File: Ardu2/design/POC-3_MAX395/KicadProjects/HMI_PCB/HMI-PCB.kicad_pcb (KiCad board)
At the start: 2 copper layers, 170.2 x 71.6 mm, 41 parts, among them P1 SplitPot_0_M, P10 TREM_VIB, P11 SplitPot_5_TR, P12 Analog Power IN, P13 Digital Power IN/OUT, P2 SEQ_SAVE, P3 SplitPot_1_A, P4 SplitPot_2_B, P5 PB_OUT, P6 Analog_Out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

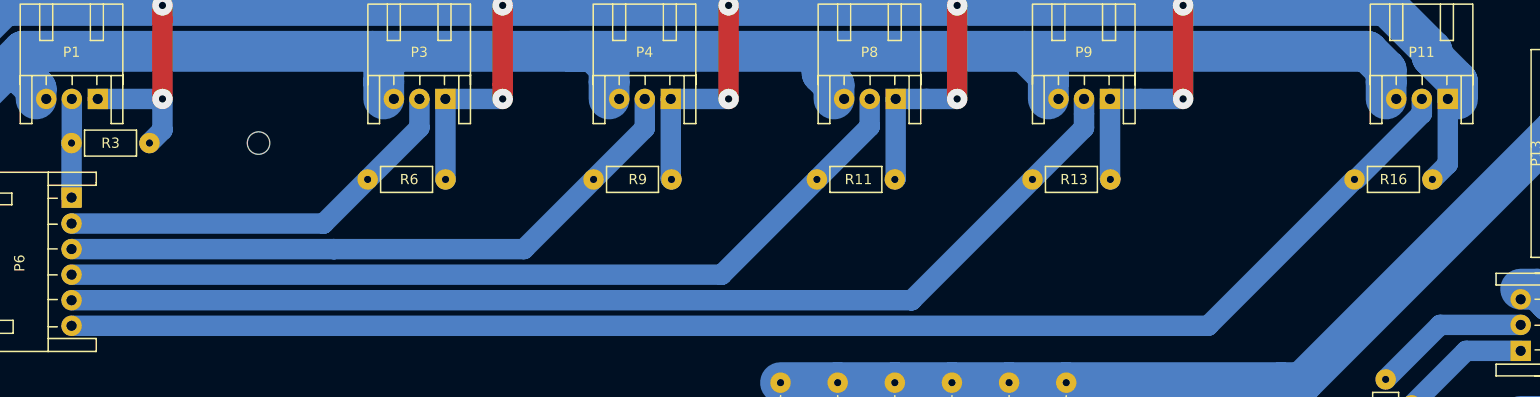
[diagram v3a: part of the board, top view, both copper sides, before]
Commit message: updated peripherals PCB
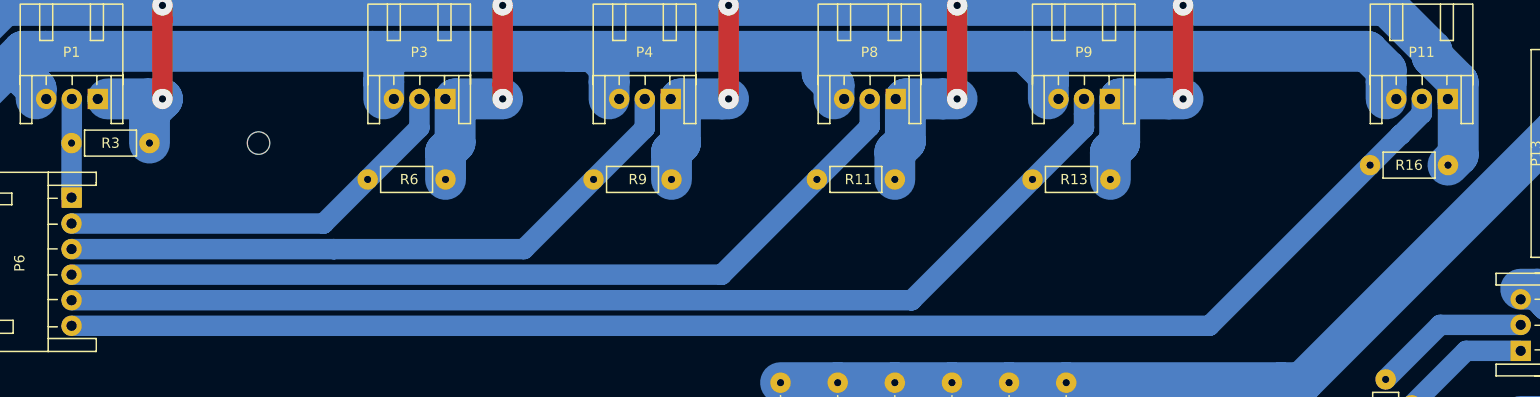
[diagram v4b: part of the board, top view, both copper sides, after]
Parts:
- moved R16 2.07 mm to (210.6, 92.3)
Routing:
- net /GND_A: track 281.5 -> 278.3 mm
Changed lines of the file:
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@@
     (thickness 1.6)
     (drawings 22)
-    (tracks 199)
+    (tracks 208)
     (zones 0)
     (modules 41)
@@
   )
   (module misc:Resistor_Horizontal_RM7mm_Big_Pads (layer F.Cu)
-    (at 209.042 93.726)
+    (at 210.566 92.329)
     (descr "Resistor, Axial,  RM 7.62mm, 1/3W,")
     (tags "Resistor Axial RM 7.62mm 1/3W R3")
@@
   (segment (start 165.5245 120.9875) (end 152.908 133.604) (width 2) (layer B.Cu) (net 7) (status 20))
   (segment (start 152.908 133.604) (end 152.908 135.641) (width 2) (layer B.Cu) (net 7) (status 30))
+  (segment (start 120.142 93.726) (end 120.142 91.041619) (width 4) (layer B.Cu) (net 8))
+  (segment (start 121.07801 90.105609) (end 121.07801 85.852) (width 4) (layer B.Cu) (net 8))
+  (segment (start 120.142 91.041619) (end 121.07801 90.105609) (width 4) (layer B.Cu) (net 8))
+  (segment (start 125.73 85.852) (end 121.07801 85.852) (width 4) (layer B.Cu) (net 8))
+  (segment (start 91.186 90.17) (end 91.186 87.122) (width 4) (layer B.Cu) (net 8))
+  (segment (start 91.186 87.122) (end 92.456 85.852) (width 4) (layer B.Cu) (net 8))
+  (segment (start 92.456 85.852) (end 91.041787 85.852) (width 4) (layer B.Cu) (net 8))
+  (segment (start 91.041787 85.852) (end 87.07801 85.852) (width 4) (layer B.Cu) (net 8))
+  (segment (start 142.24 93.726) (end 142.24 91.041619) (width 4) (layer B.Cu) (net 8))
+  (segment (start 142.24 91.041619) (end 143.11801 90.163609) (width 4) (layer B.Cu) (net 8))
+  (segment (start 143.11801 90.163609) (end 143.11801 85.852) (width 4) (layer B.Cu) (net 8))
+  (segment (start 147.828 85.852) (end 147.193 85.852) (width 4) (layer B.Cu) (net 8))
+  (segment (start 147.193 85.852) (end 143.11801 85.852) (width 4) (layer B.Cu) (net 8))
+  (segment (start 164.084 93.726) (end 164.084 91.041619) (width 4) (layer B.Cu) (net 8))
+  (segment (start 164.084 91.041619) (end 165.11801 90.007609) (width 4) (layer B.Cu) (net 8))
+  (segment (start 165.11801 90.007609) (end 165.11801 85.852) (width 4) (layer B.Cu) (net 8))
+  (segment (start 170.18 85.852) (end 168.765787 85.852) (width 4) (layer B.Cu) (net 8))
+  (segment (start 168.765787 85.852) (end 165.11801 85.852) (width 4) (layer B.Cu) (net 8))
+  (segment (start 185.166 93.726) (end 185.166 91.041619) (width 4) (layer B.Cu) (net 8))
+  (segment (start 185.166 91.041619) (end 186.078019 90.1296) (width 4) (layer B.Cu) (net 8))
+  (segment (start 186.078019 90.1296) (end 186.078019 85.852) (width 4) (layer B.Cu) (net 8))
+  (segment (start 192.278 85.852) (end 190.863787 85.852) (width 4) (layer B.Cu) (net 8))
+  (segment (start 190.863787 85.852) (end 186.078019 85.852) (width 4) (layer B.Cu) (net 8))
+  (segment (start 219.118001 84.176799) (end 219.185999 84.244797) (width 4) (layer B.Cu) (net 8))
+  (segment (start 219.185999 84.244797) (end 219.185999 91.329001) (width 4) (layer B.Cu) (net 8))
+  (segment (start 219.185999 91.329001) (end 218.186 92.329) (width 4) (layer B.Cu) (net 8))
   (segment (start 92.456 76.708) (end 76.962 76.708) (width 4) (layer B.Cu) (net 8))
   (segment (start 76.962 76.708) (end 69.881991 83.788009) (width 4) (layer B.Cu) (net 8))
   (segment (start 69.881991 83.788009) (end 69.881991 86.614) (width 4) (layer B.Cu) (net 8) (status 20))
-  (segment (start 218.168 85.852) (end 218.168 92.22) (width 2) (layer B.Cu) (net 8) (status 10))
-  (segment (start 218.168 92.22) (end 216.662 93.726) (width 2) (layer B.Cu) (net 8) (status 20))
-  (segment (start 120.128 85.852) (end 125.73 85.852) (width 2) (layer B.Cu) (net 8) (status 10))
-  (segment (start 164.168 85.852) (end 164.168 93.642) (width 2) (layer B.Cu) (net 8) (status 30))
-  (segment (start 164.168 93.642) (end 164.084 93.726) (width 2) (layer B.Cu) (net 8) (status 30))
-  (segment (start 142.168 85.852) (end 142.168 93.654) (width 2) (layer B.Cu) (net 8) (status 30))
-  (segment (start 142.168 93.654) (end 142.24 93.726) (width 2) (layer B.Cu) (net 8) (status 30))
-  (segment (start 120.128 85.852) (end 120.128 93.712) (width 2) (layer B.Cu) (net 8) (status 30))
-  (segment (start 120.128 93.712) (end 120.142 93.726) (width 2) (layer B.Cu) (net 8) (status 30))
-  (segment (start 92.456 85.852) (end 92.456 88.9) (width 2) (layer B.Cu) (net 8))
-  (segment (start 92.456 88.9) (end 91.186 90.17) (width 2) (layer B.Cu) (net 8) (status 20))
-  (segment (start 185.128 85.852) (end 185.128 93.688) (width 2) (layer B.Cu) (net 8) (status 30))
-  (segment (start 185.128 93.688) (end 185.166 93.726) (width 2) (layer B.Cu) (net 8) (status 30))
   (segment (start 212.171823 76.708) (end 216.628009 81.164186) (width 4) (layer B.Cu) (net 8))
   (segment (start 216.628009 81.164186) (end 216.628009 81.686807) (width 4) (layer B.Cu) (net 8))
@@
   (segment (start 192.278 85.852) (end 192.278 76.708) (width 2) (layer F.Cu) (net 8))
   (via (at 192.278 76.708) (size 2) (drill 0.7) (layers F.Cu B.Cu) (net 8))
-  (segment (start 188.128 85.852) (end 192.278 85.852) (width 2) (layer B.Cu) (net 8))
   (via (at 192.278 85.852) (size 2) (drill 0.7) (layers F.Cu B.Cu) (net 8))
-  (segment (start 185.128 85.852) (end 188.128 85.852) (width 2) (layer B.Cu) (net 8) (status 10))
   (segment (start 170.18 76.708) (end 147.828 76.708) (width 4) (layer B.Cu) (net 8))
   (segment (start 170.18 85.852) (end 170.18 76.708) (width 2) (layer F.Cu) (net 8))
   (via (at 170.18 76.708) (size 2) (drill 0.7) (layers F.Cu B.Cu) (net 8))
-  (segment (start 167.168 85.852) (end 170.18 85.852) (width 2) (layer B.Cu) (net 8))
   (via (at 170.18 85.852) (size 2) (drill 0.7) (layers F.Cu B.Cu) (net 8))
-  (segment (start 164.168 85.852) (end 167.168 85.852) (width 2) (layer B.Cu) (net 8) (status 10))
   (segment (start 147.828 76.708) (end 125.73 76.708) (width 4) (layer B.Cu) (net 8))
   (segment (start 147.828 85.852) (end 147.828 76.708) (width 2) (layer F.Cu) (net 8))
   (via (at 147.828 76.708) (size 2) (drill 0.7) (layers F.Cu B.Cu) (net 8))
   (via (at 147.828 85.852) (size 2) (drill 0.7) (layers F.Cu B.Cu) (net 8))
-  (segment (start 142.168 85.852) (end 147.828 85.852) (width 2) (layer B.Cu) (net 8) (status 10))
   (segment (start 125.73 76.708) (end 92.456 76.708) (width 4) (layer B.Cu) (net 8))
   (segment (start 125.73 84.437787) (end 125.73 76.708) (width 2) (layer F.Cu) (net 8))
@@
   (segment (start 125.73 85.852) (end 125.73 84.437787) (width 2) (layer F.Cu) (net 8))
   (via (at 125.73 85.852) (size 2) (drill 0.7) (layers F.Cu B.Cu) (net 8))
-  (segment (start 86.128 85.852) (end 92.456 85.852) (width 2) (layer B.Cu) (net 8) (status 10))
   (segment (start 92.456 78.122213) (end 92.456 85.852) (width 2) (layer F.Cu) (net 8))
   (via (at 92.456 85.852) (size 2) (drill 0.7) (layers F.Cu B.Cu) (net 8))
@@
   (segment (start 182.588009 88.683991) (end 182.588009 87.297609) (width 2) (layer B.Cu) (net 16))
   (segment (start 182.588009 87.297609) (end 182.588009 85.852) (width 2) (layer B.Cu) (net 16) (status 20))
-  (segment (start 83.566 108.0405) (end 194.7275 108.0405) (width 2) (layer B.Cu) (net 17) (status 10))
-  (segment (start 194.7275 108.0405) (end 209.042 93.726) (width 2) (layer B.Cu) (net 17) (status 20))
-  (segment (start 215.628 87.266213) (end 215.628 85.852) (width 2) (layer B.Cu) (net 17) (status 20))
-  (segment (start 209.199618 93.726) (end 215.628 87.297618) (width 2) (layer B.Cu) (net 17) (status 10))
+  (segment (start 210.566 92.329) (end 213.55299 89.34201) (width 2) (layer B.Cu) (net 17))
+  (segment (start 213.55299 89.34201) (end 213.583608 89.34201) (width 2) (layer B.Cu) (net 17))
+  (segment (start 213.583608 89.34201) (end 215.628 87.297618) (width 2) (layer B.Cu) (net 17))
   (segment (start 215.628 87.297618) (end 215.628 87.266213) (width 2) (layer B.Cu) (net 17))
+  (segment (start 215.628 87.266213) (end 215.628 85.852) (width 2) (layer B.Cu) (net 17))
+  (segment (start 83.566 108.0405) (end 194.8545 108.0405) (width 2) (layer B.Cu) (net 17))
+  (segment (start 194.8545 108.0405) (end 210.566 92.329) (width 2) (layer B.Cu) (net 17))
   (segment (start 225.298 120.396) (end 222.359787 120.396) (width 2) (layer B.Cu) (net 18) (status 10))
   (segment (start 222.359787 120.396) (end 218.186 124.569787) (width 2) (layer B.Cu) (net 18))

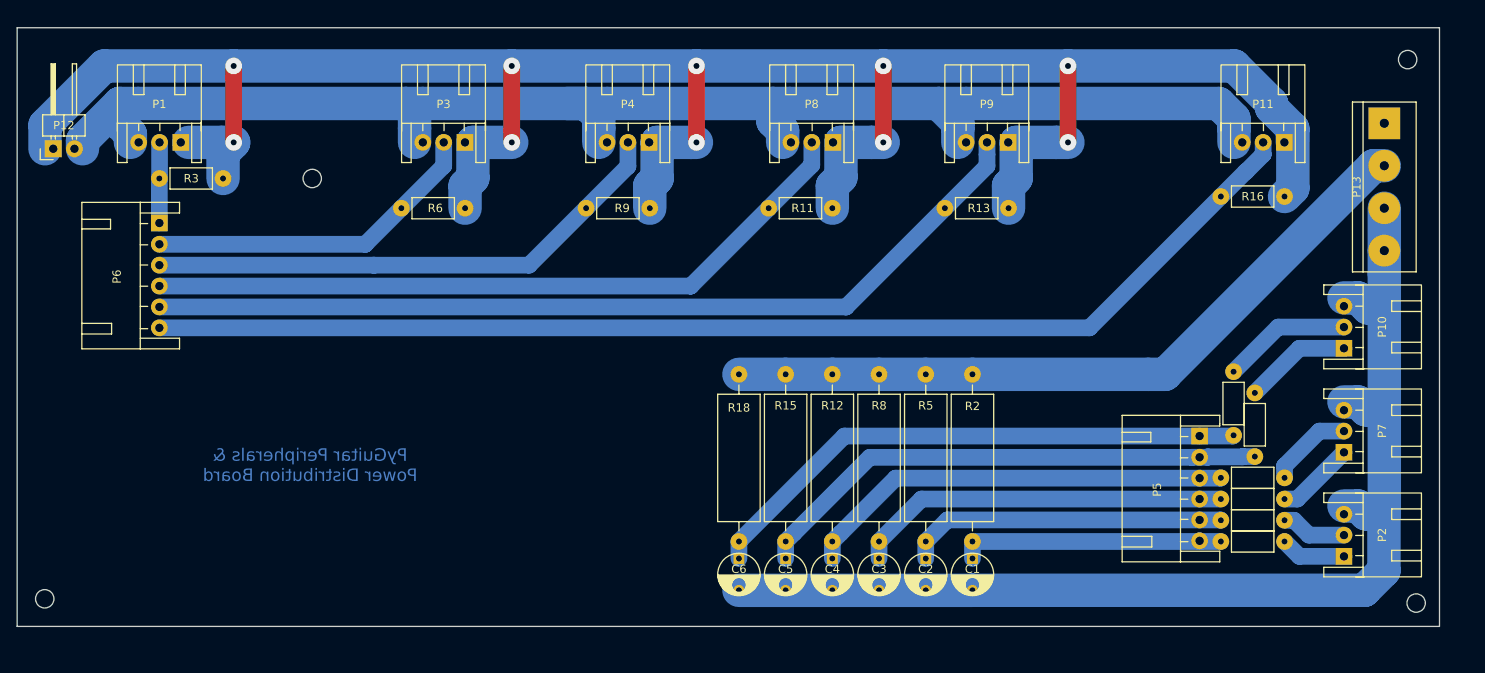
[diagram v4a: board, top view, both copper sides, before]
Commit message: updated peripherals PCB
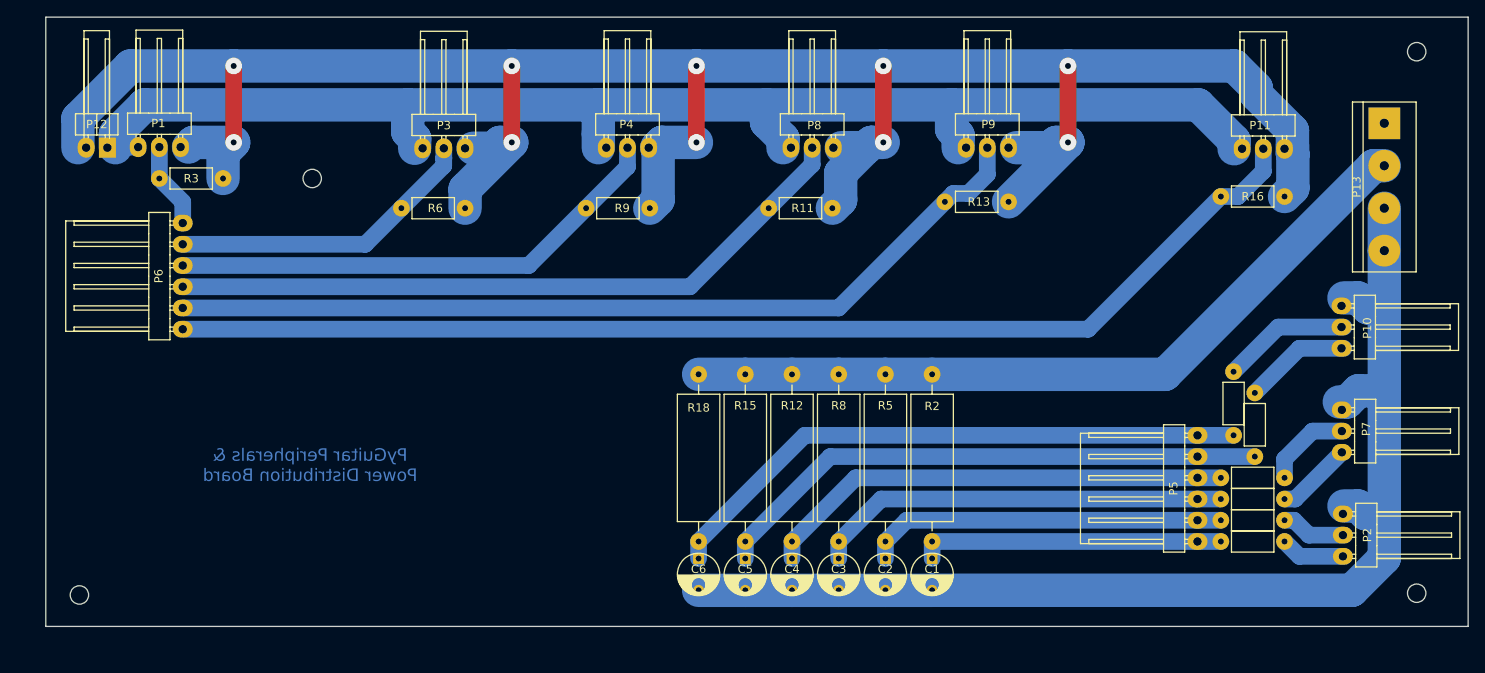
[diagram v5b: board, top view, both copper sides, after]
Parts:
- P1, P10, P11, P2, P3, P4, P7, P8, P9: footprint misc:Wafer_Horizontal10x5.8x7RM2.5-3_1mmHole -> misc:Wafer_Angled_1x03_1mm_hole
- P12: footprint misc:Pin_Header_Angled_1x02_1mm_hole -> misc:Wafer_Angled_1x02_1mm_hole
- P5, P6: footprint misc:Wafer_Horizontal17.5x5.8x7RM2.5-6_1mm_Hole -> misc:Wafer_Angled_1x06_1mm_Hole
- moved P6 13.0 mm to (86.4, 108.2), turned to 180 degrees
- moved P5 12.6 mm to (207.8, 133.6), turned to 180 degrees
- moved P4 5.17 mm to (137.0, 86.5), turned to 90 degrees
- moved P1 5.13 mm to (81.0, 86.4), turned to 90 degrees
- moved P11 5.12 mm to (213.1, 86.6), turned to 90 degrees
- moved P3 5.12 mm to (115.1, 86.6), turned to 90 degrees
- moved P10 5.09 mm to (225.0, 105.4), turned to 0 degrees
- moved P7 5.09 mm to (225.0, 117.9), turned to 0 degrees
- moved P9 5.08 mm to (180.1, 86.5), turned to 90 degrees
- moved P2 5.08 mm to (225.2, 130.3), turned to 0 degrees
- moved P8 5.08 mm to (159.1, 86.5), turned to 90 degrees
- moved C1 4.83 mm to (176.0, 136.3)
- moved C5 4.83 mm to (153.7, 136.3)
- moved R15 4.83 mm to (153.7, 113.6)
- moved R2 4.83 mm to (176.0, 113.6)
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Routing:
- net /3v3_A: track 173.1 -> 165.1 mm
- net /X7: track 62.4 -> 67.2 mm
- net /X22: track 66.5 -> 71.3 mm
- net /Y5: track 45.0 -> 49.9 mm
- net /Y6: track 51.7 -> 56.5 mm
- net /3v3_D: track 87.6 -> 92.4 mm
- net /Y4: track 38.4 -> 43.2 mm
- net /Y3: track 31.8 -> 36.6 mm
- net /GND_D: track 137.5 -> 142.0 mm
- net /X2: track 40.7 -> 37.2 mm
- net /X3: track 63.8 -> 60.4 mm
- net /X4: track 86.8 -> 83.4 mm
- net /Y11: track 108.8 -> 106.1 mm
- net /GND_A: track 278.3 -> 280.9 mm
- net /Y12: track 142.1 -> 139.8 mm
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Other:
- board size 170.2 x 71.6 mm -> 170.2 x 72.9 mm

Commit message: updated to HMI PCB after SENSEI review
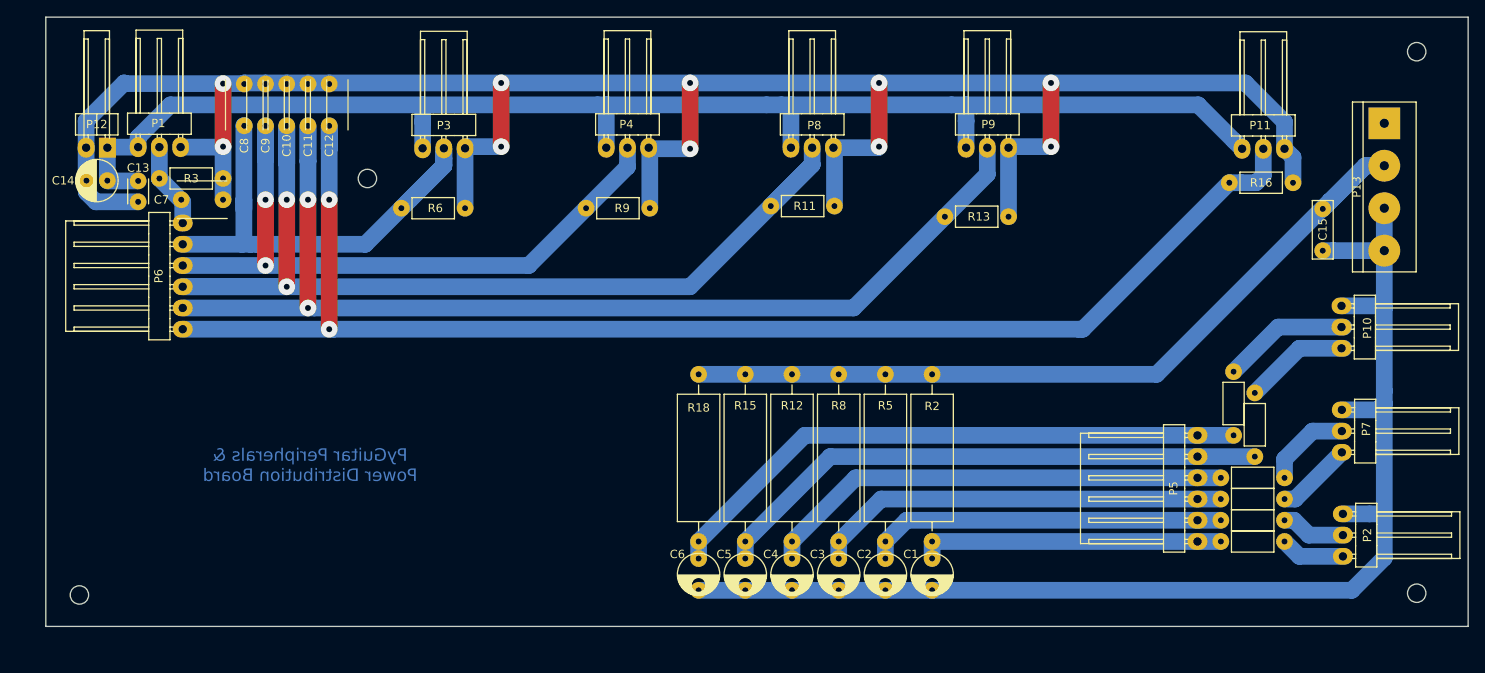
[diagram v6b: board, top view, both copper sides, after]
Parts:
- added C10: 10nF, misc:C_Disc_D6_P5_2mm_Pad_0_7mm_hole, F.Cu at (98.8, 78.9)
- added C11: 10nF, misc:C_Disc_D6_P5_2mm_Pad_0_7mm_hole, F.Cu at (101.3, 78.9)
- added C12: 10nF, misc:C_Disc_D6_P5_2mm_Pad_0_7mm_hole, F.Cu at (103.9, 78.9)
- added C13: 100nF, Capacitors_ThroughHole:C_Disc_D3_P2.5, F.Cu at (81.0, 93.0)
- added C14: 10µF, Capacitors_ThroughHole:C_Radial_D5_L11_P2.5, F.Cu at (77.3, 90.4)
- added C15: 22nF, Capacitors_ThroughHole:C_Rect_L7_W2.5_P5, F.Cu at (222.8, 93.8)
- added C7: 10nF, misc:C_Disc_D6_P5_2mm_Pad_0_7mm_hole, F.Cu at (91.2, 92.7)
- added C8: 10nF, misc:C_Disc_D6_P5_2mm_Pad_0_7mm_hole, F.Cu at (93.7, 78.9)
- added C9: 10nF, misc:C_Disc_D6_P5_2mm_Pad_0_7mm_hole, F.Cu at (96.3, 78.9)
- C1, C2, C3, C4, C5, C6: footprint misc:C_Radial_D5_L11_P3.81_0_7mm_Hole -> misc:C_Radial_D5_L11_P3.81_pads_2_mm_holes_7mm
- moved REF** 6.60 mm to (108.5, 90.2)
- moved R16 1.94 mm to (211.6, 90.7)
- moved R13 1.78 mm to (177.5, 94.7)
- moved R11 0.36 mm to (156.7, 93.5)
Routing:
- net /X4: track 83.4 -> 126.5 mm, vias 0 -> 2
- net /Y12: track 139.8 -> 167.0 mm, vias 0 -> 2
- net /Y11: track 106.1 -> 132.0 mm, vias 0 -> 2
- net /X2: track 37.2 -> 62.0 mm
- net /X3: track 60.4 -> 81.0 mm, vias 0 -> 2
- net /GND_A: track 280.9 -> 269.9 mm
- net /3v3_D: track 92.4 -> 101.9 mm
- net /GND_D: track 142.0 -> 148.4 mm
- net /3v3_A: track 165.1 -> 169.1 mm
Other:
- board text added: "J6"
- board text added: "J7"
- board text added: "J8"
- board text added: "J9"

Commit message: updated to HMI PCB after second SENSEI review
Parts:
- added C16: 1µF, Capacitors_ThroughHole:C_Radial_D5_L6_P2.5, F.Cu at (74.5, 94.6)
- added L1: 10mH, Resistors_ThroughHole:Resistor_Horizontal_RM10mm, F.Cu at (77.3, 100.1)
- P6: value Analog_Out -> Analog_Signal_Out
- moved C14 10.0 mm to (74.5, 100.1)
- moved C13 9.48 mm to (72.0, 90.0), turned to 0 degrees
- moved P6 9.27 mm to (86.4, 117.5)
- moved R13 4.06 mm to (177.5, 90.7)
- moved REF** 3.58 mm to (108.8, 86.6)
- moved R6 3.05 mm to (112.5, 90.7)
- moved R9 3.05 mm to (134.6, 90.7)
- moved R11 2.79 mm to (156.7, 90.7)
- moved R16 1.02 mm to (210.6, 90.7)
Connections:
- P12 pad 2: /3v3_A -> /3v3_A_IN
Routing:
- net /3v3_A: track 169.1 -> 185.7 mm
- net /X4: track 126.5 -> 110.4 mm
- net /GND_A: track 269.9 -> 259.9 mm
- net /X1: track 10.3 -> 19.5 mm
- net /X2: track 62.0 -> 56.5 mm
- net /X3: track 81.0 -> 85.1 mm
- net /3v3_A_IN: track 0.00 -> 3.43 mm
- net /Y11: track 132.0 -> 134.7 mm
- net /Y12: track 167.0 -> 169.1 mm
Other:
- board text added: "3v3_A_IN"
- board text removed: "3v3_A"
